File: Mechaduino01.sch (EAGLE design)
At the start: 57 parts, among them IC1 SAMD21G18A-AUT, IC2 AP2112K-3.3, Q1 2.5A/30V, Q2 NFET, SW1 SPST_TACT-KMR2, U3 74AHC1G125, Y1 32,768Khz

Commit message: hardwired encoder, driver
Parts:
- removed JP10, JP11: (no value), SparkFun-Connectors:M07
- removed JP3: SPI, Arduino-Neutrino-082:CONNETTORI_0114_PH254-203DF118A00V
- removed JP5: (no value), SparkFun-Connectors:M06SILK_FEMALE_PTH
- removed POWERCONNECTOR: (no value), SparkFun-Connectors:M025MM
- removed SJ1: (no value), jumper:SJ
- added MOTOR_POWER: (no value), SparkFun-Connectors:M025MM
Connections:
- removed net ARDUINO_D4: IC1.PA8/I2C/AIN16/SCOM2PAD0+/TC0, JP1.12
- removed net ARDUINO_D5: IC1.PA15/XOUT/EIC/SCOM2PAD3+/TC3, JP1.13
- removed net ARDUINO_D6: IC1.PA20/EIC/SCOM5PAD2+, JP1.14
- removed net ARDUINO_D7: IC1.PA21/EIC/SCOM5PAD3+, JP2.1
- removed net ARDUINO_D8: IC1.PA6/EIC/AIN6/SCOM0PAD2/TC1, JP2.2
- removed net ARDUINO_D9: IC1.PA7/EIC/AIN7/SCOM0PAD3/TC1, JP2.3
- removed net N$10: JP5.4, U$1.IN2
- removed net N$11: JP5.5, U$1.IN1
- removed net N$12: JP5.6, R14.1
- removed net N$17: JP10.1, U$4.CSN
- removed net N$18: JP10.2, U$4.CLK
- removed net N$19: JP10.3, U$4.MISO
- removed net N$20: JP10.4, U$4.MOSI
- removed net N$21: JP5.1, R15.1
- removed net N$22: JP10.6, U$4.A
- removed net N$23: JP10.7, U$4.B
- removed net N$24: JP11.1, U$4.W
- removed net N$25: JP11.2, U$4.V
- removed net N$26: JP11.3, U$4.U
- removed net N$28: C17.1, JP11.5, U$4.VDD3V
- removed net N$29: JP11.6, U$4.GND
- removed net N$30: JP11.7, U$4.I
- removed net N$5: C12.+, C13.1, POWERCONNECTOR.1, U$1.VBB, U$1.VBB2
- removed net N$8: JP5.2, U$1.IN3
- removed net N$9: JP5.3, U$1.IN4
- removed net PB10_S4_SPI_MOSI: IC1.PB10/EIC/SCOM4PAD2/TC5, JP3.4
- removed net PB11_S4_SPI_SCK: IC1.PB11/EIC/SCOM4PAD3/TC5, JP3.3
- removed net PB12_S4_SPI_MISO: IC1.PA12/I2C/EIC/SCOM2PAD0+/TC2, JP3.1
- new net ARDUINO_D4----VREF2: IC1.PA8/I2C/AIN16/SCOM2PAD0+/TC0, JP1.12, R15.1
- new net ARDUINO_D5----IN3: IC1.PA15/XOUT/EIC/SCOM2PAD3+/TC3, JP1.13, U$1.IN3
- new net ARDUINO_D6----IN4: IC1.PA20/EIC/SCOM5PAD2+, JP1.14, U$1.IN4
- new net ARDUINO_D7----IN2: IC1.PA21/EIC/SCOM5PAD3+, JP2.1, U$1.IN2
- new net ARDUINO_D8----IN1: IC1.PA6/EIC/AIN6/SCOM0PAD2/TC1, JP2.2, U$1.IN1
- new net ARDUINO_D9----VREF1: IC1.PA7/EIC/AIN7/SCOM0PAD3/TC1, JP2.3, R14.1
- new net HEADER_MISO: IC1.PA12/I2C/EIC/SCOM2PAD0+/TC2, U$4.MISO
- new net HEADER_MOSI: IC1.PB10/EIC/SCOM4PAD2/TC5, U$4.MOSI
- new net HEADER_SCK: IC1.PB11/EIC/SCOM4PAD3/TC5, U$4.CLK
- new net HEADER_SS: U$4.CSN
- new net V+: C12.+, C13.1, MOTOR_POWER.1, U$1.VBB, U$1.VBB2
- net 3.3V: now also C17.1, U$4.VDD3V; no longer JP3.2, SJ1.2
- net GND: now also U$4.GND; no longer JP10.5, JP3.6
- net GND2: now also MOTOR_POWER.2; no longer POWERCONNECTOR.2
- net N$27: no longer JP11.4
- net RESET: no longer JP3.5
- net VIN: no longer SJ1.1
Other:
- note added: "A4954"
- note removed: "If USB power is available, VOUT = USB; otherwise VOUT = VIN."
- note removed: "USB / Voltage Regulator"
- note removed: "VOUT is the output of the TPS2115 and is actively limited to 500mA."
- moved on the sheet: C1, C11, C12, C13, C14, C15, C16, C17, C2, C3, C4, C5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

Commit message: formatted and added license
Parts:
- added FRAME1: FRAME-LEDGER, SparkFun-Aesthetics:FRAME-LEDGER
- added LOGO4: OSHW-LOGOL, SparkFun-Aesthetics:OSHW-LOGOL
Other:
- note added: "1.0"
- note added: "Arduino Zero Compatible"
- note added: "Based on: Arduino Zero by Arduino.cc Arduino M0 by Arduino.org Neutrino by Rabidprototypes.com SAMD21 Dev Breakout by Sparkfun.com"
- note added: "Joe Church"
- note added: "SAMD21"
- note removed: "Arduino Zero"
- moved on the sheet: C1, C10, C11, C12, C13, C14, C15, C16, C17, C2, C3, C4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

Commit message: ready for layout
ripped up old stuff, shrunk to 1.65" square from 1.7" and moved
placement sensitive parts accordingly
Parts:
- removed JP1, JP2: M14NOSILK_SMALLPADS, SparkFun-Connectors:M14NOSILK_SMALLPADS
- added 3V3, GND, V+, VIN: (no value), SparkFun-Connectors:M031X03_NO_SILK
- added JP3: (no value), SparkFun-Connectors:M10NO_SILK_PTH_FEMALE
- added JP5: (no value), SparkFun-Connectors:M06NO_SILK_FEMALE_PTH
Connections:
- removed net ARDUINO_A2: IC1.PB9/EIC/AIN3/SCOM4PAD1//TC4, JP1.4
- removed net HEADER_SS: U$4.CSN
- removed net VBUS: JP2.12
- removed net VOUT: JP2.11
- new net ARDUINO_A2----HEADER_SS: IC1.PB9/EIC/AIN3/SCOM4PAD1//TC4, U$4.CSN
- net 3.3V: now also 3V3.1, 3V3.2, 3V3.3; no longer JP2.10
- net ARDUINO_A0: now also JP3.2; no longer JP1.2
- net ARDUINO_A1: now also JP3.3; no longer JP1.3
- net ARDUINO_A3: now also JP3.4; no longer JP1.5
- net ARDUINO_A4: now also JP3.5; no longer JP1.6
- net ARDUINO_A5: now also JP3.6; no longer JP1.7
- net ARDUINO_AREF: now also JP3.1; no longer JP1.1
- net ARDUINO_D0: now also JP3.7; no longer JP1.8
- net ARDUINO_D1: now also JP3.8; no longer JP1.9
- net ARDUINO_D10_SS: now also JP5.1; no longer JP2.4
- net ARDUINO_D11_MOSI: now also JP5.2; no longer JP2.5
- net ARDUINO_D12_MISO: now also JP5.3; no longer JP2.6
- net ARDUINO_D13_SCK: now also JP5.4; no longer JP2.7
- net ARDUINO_D2: now also JP3.9; no longer JP1.10
- net ARDUINO_D20_SDA: now also JP5.5; no longer JP2.8
- net ARDUINO_D21_SCL: now also JP5.6; no longer JP2.9
- net ARDUINO_D3: now also JP3.10; no longer JP1.11
- net ARDUINO_D4----VREF2: no longer JP1.12
- net ARDUINO_D5----IN3: no longer JP1.13
- net ARDUINO_D6----IN4: no longer JP1.14
- net ARDUINO_D7----IN2: no longer JP2.1
- net ARDUINO_D8----IN1: no longer JP2.2
- net ARDUINO_D9----VREF1: no longer JP2.3
- net GND: now also GND.1, GND.2, GND.3; no longer JP2.13
- net V+: now also V+.1, V+.2, V+.3
- net VIN: now also VIN.1, VIN.2, VIN.3; no longer JP2.14
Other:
- note added: "0.1"
- note added: "Mechaduino"
- note removed: "1.0"
- moved on the sheet: C1, C11, C2, C3, C4, C5, C7, C8, IC1, JP4, L2, R6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

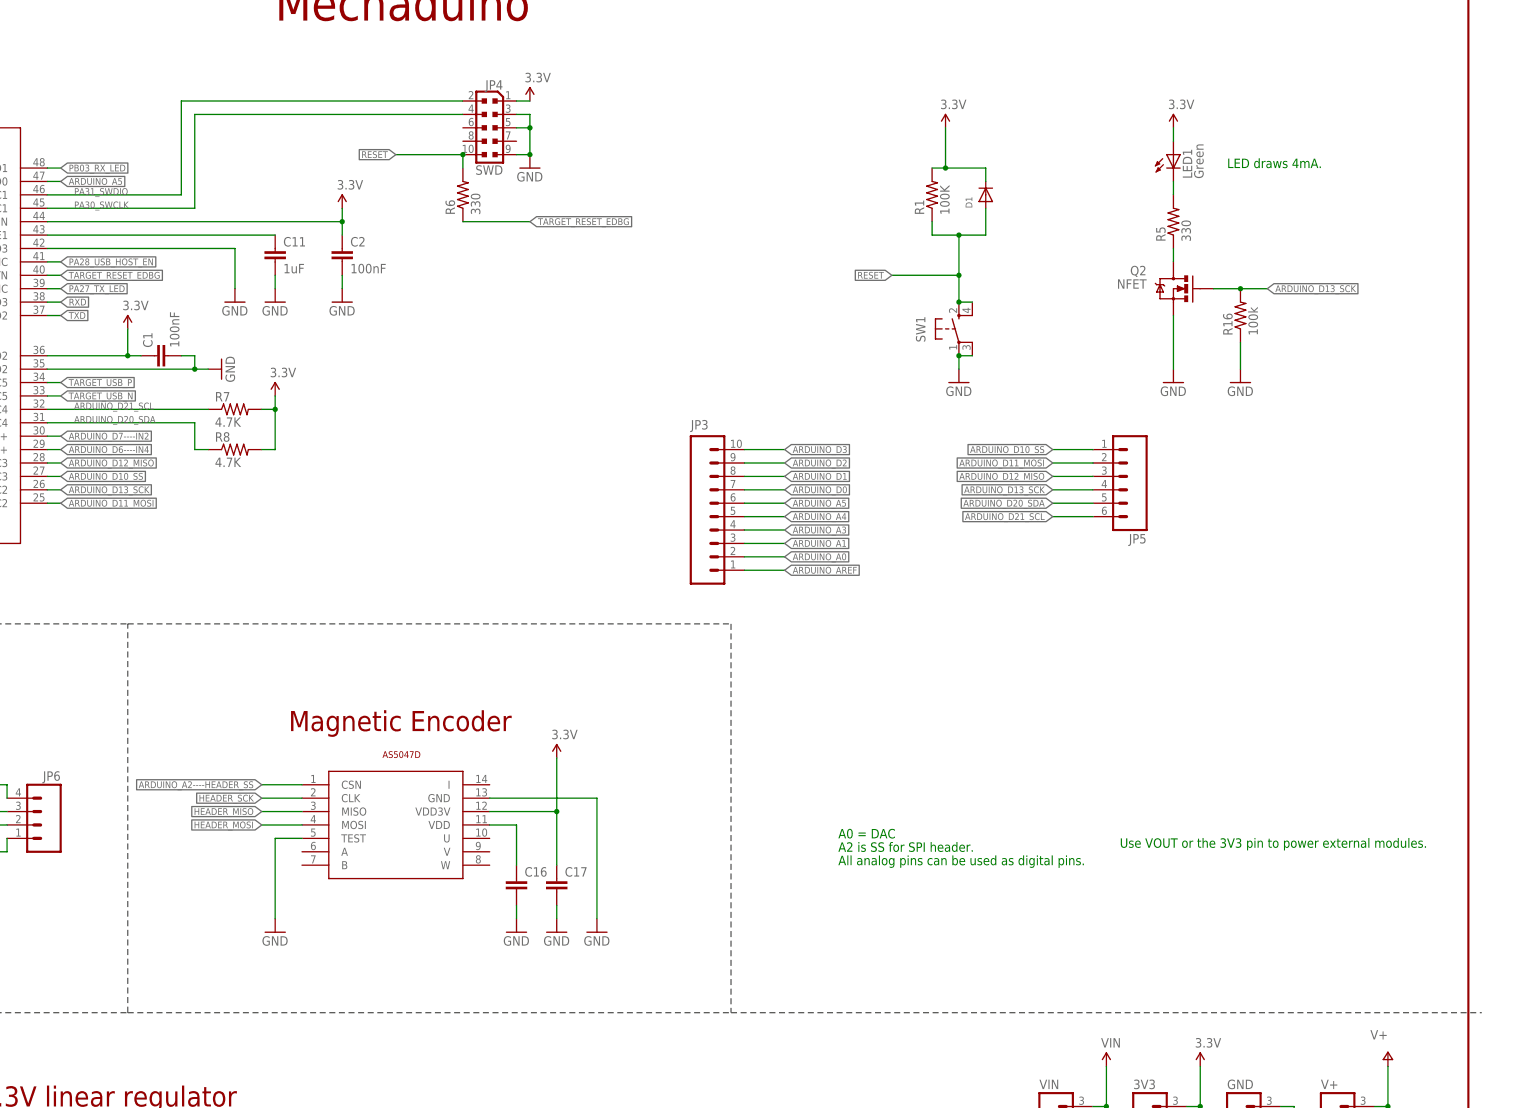
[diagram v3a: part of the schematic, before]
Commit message: added level shifter
on D0, D1
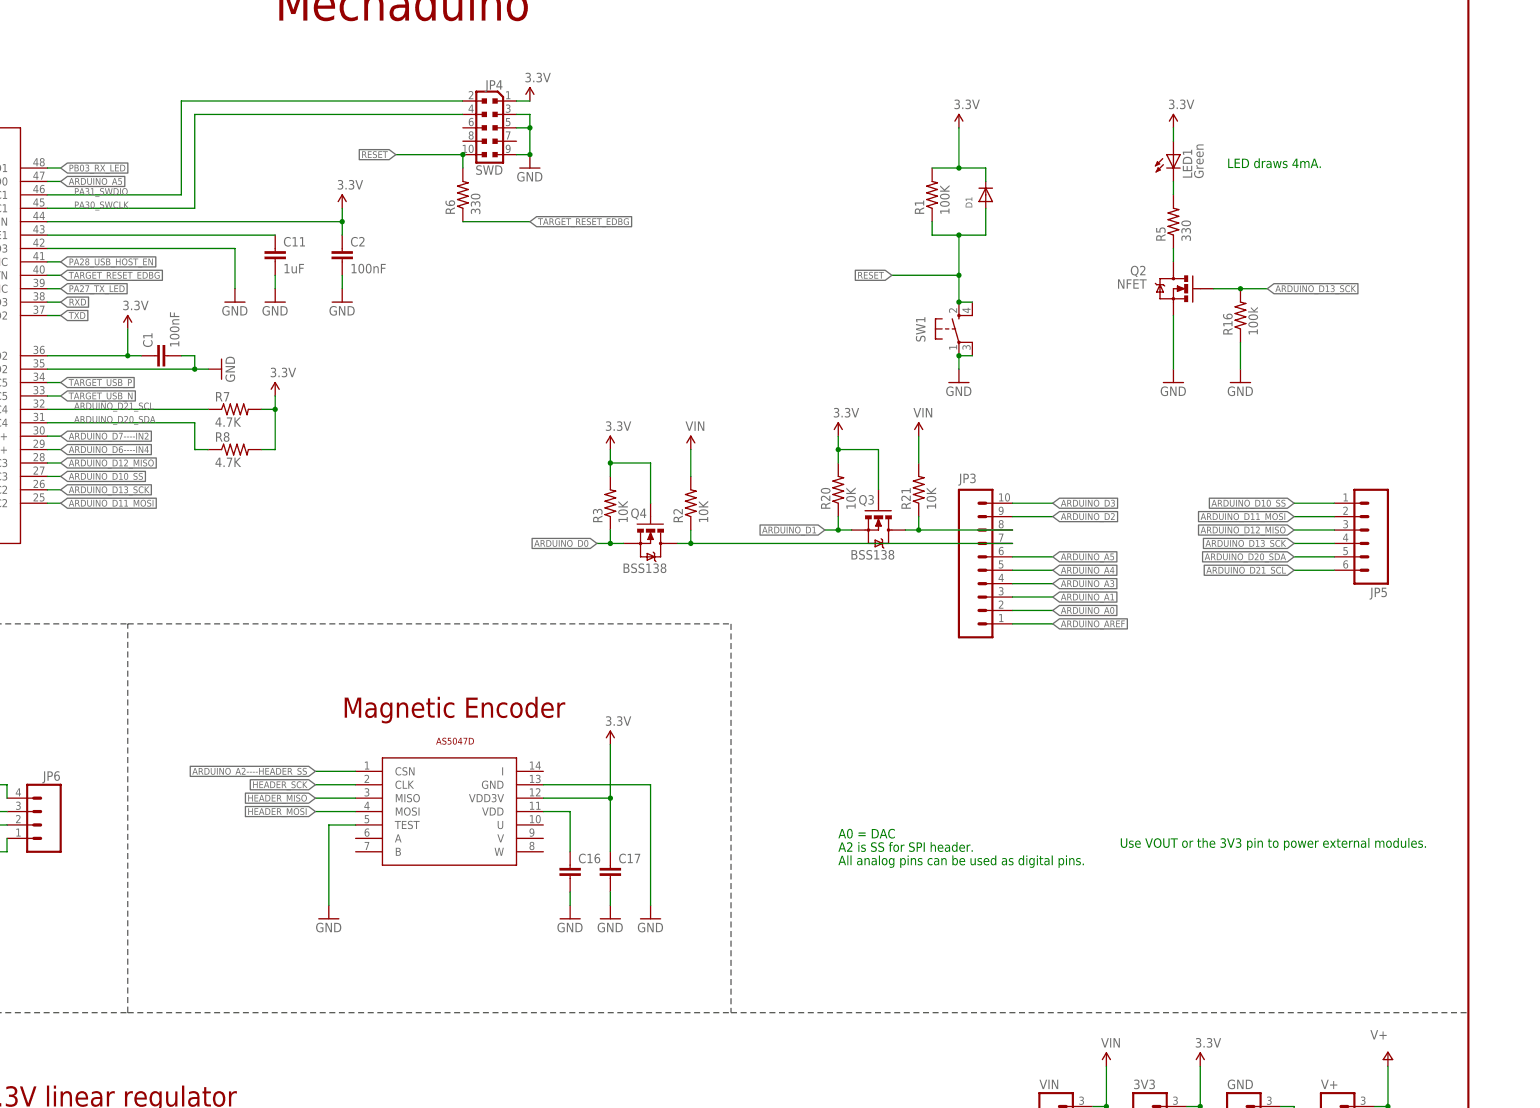
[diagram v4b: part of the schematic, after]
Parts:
- added Q3, Q4: BSS138, SparkFun:MOSFET-NCHANNELSMD
- added R2, R20, R21, R3: 10K, adafruit:R-US_R0402-VISHAY
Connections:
- new net HV1: JP3.8, Q3.D, R21.1
- new net HV2: JP3.7, Q4.D, R2.1
- net 3.3V: now also Q3.G, Q4.G, R20.2, R3.2
- net ARDUINO_D0: now also Q4.S, R3.1; no longer JP3.7
- net ARDUINO_D1: now also Q3.S, R20.1; no longer JP3.8
- net VIN: now also R2.2, R21.2
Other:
- moved on the sheet: C16, C17, JP3, JP5

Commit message: replaced through hole passives with smd
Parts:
- added C18: 10.0uF, swift:CAP0402
- added C19: 0.1uF, swift:CAP0402
- added C6: 0.01uF, swift:CAP0402
- C1, C2, C3, C4, C5: value 100nF -> 0.1uF
- C10: value 2.2uF -> 10.0uF
- C12: device SparkFun-Capacitors:CAP_POLPTH1 -> SparkFun-Capacitors:CAP_POLD
- C13: value 0.22uF -> 1.0uF; device SparkFun-Capacitors:CAPEZ -> swift:CAP0603
- C14, C15: value (none) -> 0.1uF; device resistor:C-US050-035X075 -> swift:CAP0402
- C16: value (none) -> 0.1uF
- C9: value 1uF -> 0.1uF
- L1, L2: value (none) -> BLM18PG471SN1D
- R12, R13: device resistor:R-US_0204/2V -> adafruit:R-US_R1206
- R14, R15: device resistor:R-US_0204/2V -> adafruit:R-US_R0402-VISHAY
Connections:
- net 3.3V: now also C19.1
- net GND: now also C18.2, C19.2
- net GND2: now also C6.2
- net V+: now also C6.1
- net VIN: now also C18.1
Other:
- moved on the sheet: C14, C15

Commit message: routed?
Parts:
- removed JP3: (no value), SparkFun-Connectors:M10NO_SILK_PTH_FEMALE
- removed JP5: (no value), SparkFun-Connectors:M06NO_SILK_FEMALE_PTH
- added J2: (no value), MF_Connectors:HEADER_01X10_PTH_2.54MM
- added J3: (no value), MF_Connectors:HEADER_01X06_PTH_2.54MM
- 3V3, GND, V+, VIN: device SparkFun-Connectors:M031X03_NO_SILK -> MF_Connectors:HEADER_01X03_PTH_2.54MM
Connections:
- net 3.3V: now also 3V3.PIN0, 3V3.PIN1, 3V3.PIN2; no longer 3V3.1, 3V3.2, 3V3.3
- net ARDUINO_A0: now also J2.PIN8; no longer JP3.2
- net ARDUINO_A1: now also J2.PIN7; no longer JP3.3
- net ARDUINO_A3: now also J2.PIN6; no longer JP3.4
- net ARDUINO_A4: now also J2.PIN5; no longer JP3.5
- net ARDUINO_A5: now also J2.PIN4; no longer JP3.6
- net ARDUINO_AREF: now also J2.PIN9; no longer JP3.1
- net ARDUINO_D10_SS: now also J3.PIN0; no longer JP5.1
- net ARDUINO_D11_MOSI: now also J3.PIN1; no longer JP5.2
- net ARDUINO_D12_MISO: now also J3.PIN2; no longer JP5.3
- net ARDUINO_D13_SCK: now also J3.PIN3; no longer JP5.4
- net ARDUINO_D2: now also J2.PIN1; no longer JP3.9
- net ARDUINO_D20_SDA: now also J3.PIN4; no longer JP5.5
- net ARDUINO_D21_SCL: now also J3.PIN5; no longer JP5.6
- net ARDUINO_D3: now also J2.PIN0; no longer JP3.10
- net GND: now also GND.PIN0, GND.PIN1, GND.PIN2; no longer GND.1, GND.2, GND.3
- net HV1: now also J2.PIN2; no longer JP3.8
- net HV2: now also J2.PIN3; no longer JP3.7
- net V+: now also V+.PIN0, V+.PIN1, V+.PIN2; no longer V+.1, V+.2, V+.3
- net VIN: now also VIN.PIN0, VIN.PIN1, VIN.PIN2; no longer VIN.1, VIN.2, VIN.3

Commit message: reviewed
updated graphics, checked stuff... done?
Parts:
- added U$5: MECHADUINO_LOGO, stepper_servo_prototype_1:MECHADUINO_LOGO
- C17: value (none) -> 1uF
- J3: LABEL00 D10 SS -> SS D10; LABEL01 D11 MOSI -> MOSI D11; LABEL02 D12 MISO -> MISO D12; LABEL03 D13 SCK -> SCK D13; LABEL04 D20 SDA -> SDA D20; LABEL05 D21 SCL -> SCL D21
- LOGO4: value OSHW-LOGOL -> OSHW-LOGOL-COPPER; device SparkFun-Aesthetics:OSHW-LOGOL -> SparkFun-Aesthetics:OSHW-LOGOL-COPPER
- R14, R15: value (none) -> 1k
- U$3: value TROPICAL_LABS_LOGO_1LOGO2 -> TROPICAL_LABS_LOGO_1LOGO3; device stepper_servo_prototype_1:TROPICAL_LABS_LOGO_1LOGO2 -> stepper_servo_prototype_1:TROPICAL_LABS_LOGO_1LOGO3
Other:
- moved on the sheet: SH1
